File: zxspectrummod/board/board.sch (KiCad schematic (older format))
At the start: 7 parts, among them IC1 LVC245A, IC2 LVC245A

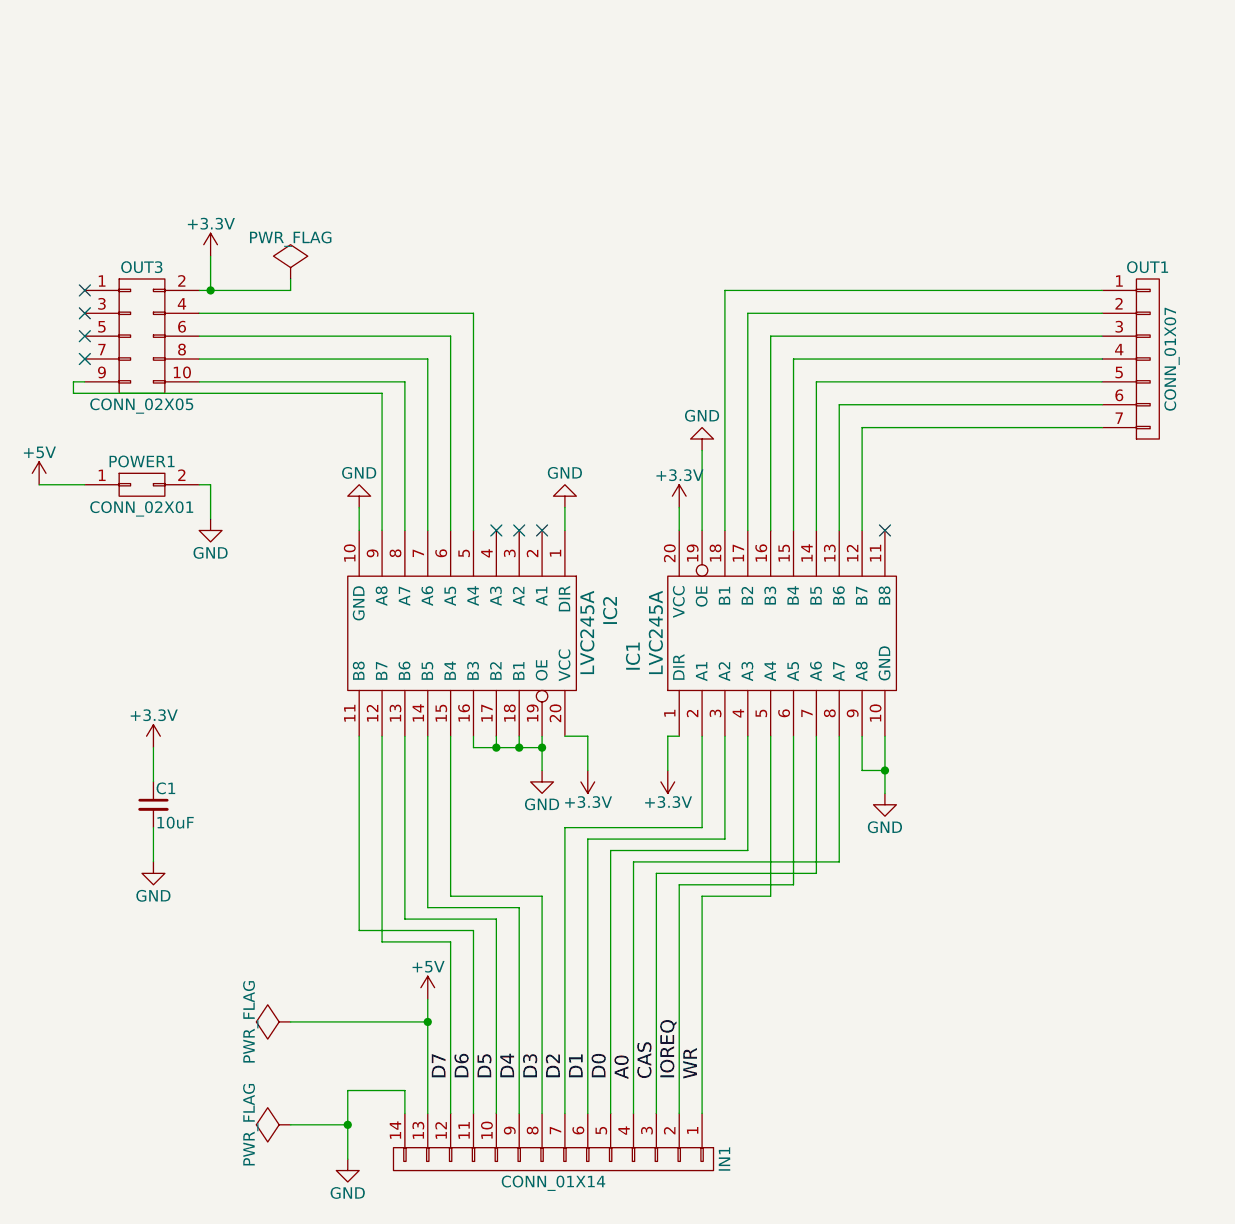
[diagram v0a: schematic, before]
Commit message: small additions for zx spectrum mod
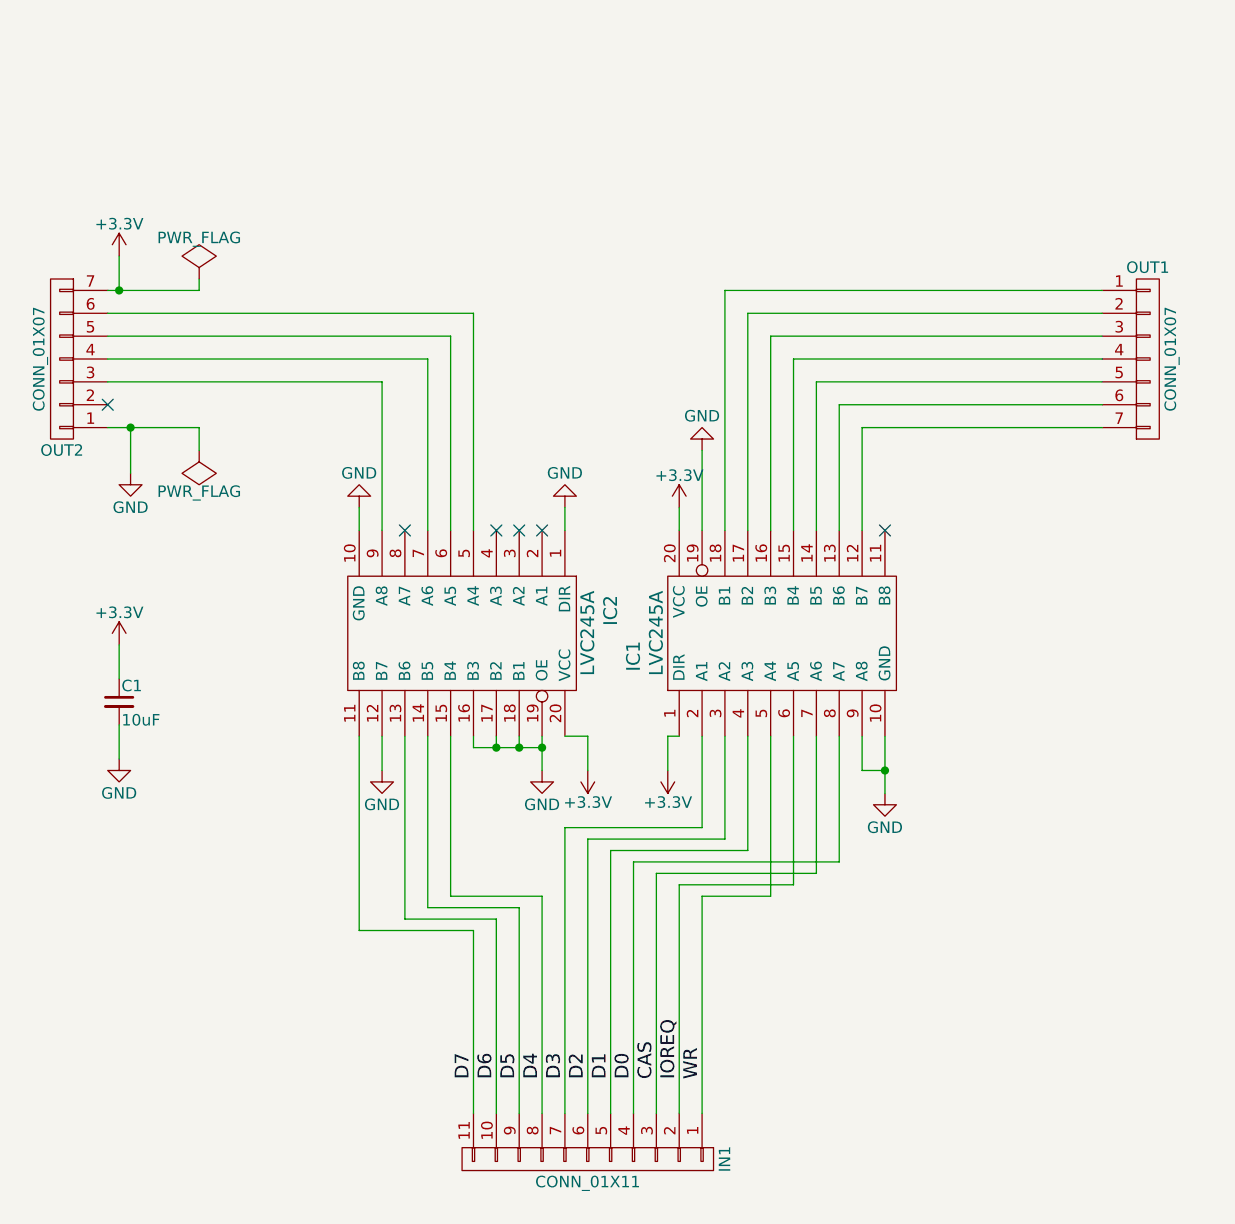
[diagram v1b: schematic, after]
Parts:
- removed IN1: CONN_01X14, Pin_Headers:Pin_Header_Straight_1x14_Pitch2.54mm, symbol CONN_01X14
- removed OUT3: CONN_02X05, Pin_Headers:Pin_Header_Straight_2x05_Pitch2.54mm, symbol CONN_02X05
- removed POWER1: CONN_02X01, Pin_Headers:Pin_Header_Straight_2x01_Pitch2.54mm, symbol CONN_02X01
- added IN1: CONN_01X11, Pin_Headers:Pin_Header_Straight_1x11_Pitch2.54mm, symbol CONN_01X11
- added OUT2: CONN_01X07, Pin_Headers:Pin_Header_Straight_1x07_Pitch2.54mm, symbol CONN_01X07
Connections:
- net A0 is gone; now on net D0: IC1.8 (A7)
- net +3V3: now also OUT2.7 (P7)
- net CAS: now also IN1.3 (P3)
- net D0: now also IN1.4 (P4); no longer IC1.4 (A3)
- net D1: now also IC1.4 (A3), IN1.5 (P5); no longer IC1.3 (A2)
- net D2: now also IC1.3 (A2), IN1.6 (P6); no longer IC1.2 (A1)
- net D3: now also IC1.2 (A1), IN1.7 (P7); no longer IC2.15 (B4)
- net D4: now also IC2.15 (B4), IN1.8 (P8); no longer IC2.14 (B5)
- net D5: now also IC2.14 (B5), IN1.9 (P9); no longer IC2.13 (B6)
- net D6: now also IC2.13 (B6), IN1.10 (P10); no longer IC2.11 (B8)
- net D7: now also IC2.11 (B8), IN1.11 (P11); no longer IC2.12 (B7)
- net GND: now also IC2.12 (B7), OUT2.1 (P1)
- net IOREQ: now also IN1.2 (P2)
- net WR: now also IN1.1 (P1)
- net at IC2.5 (A4): now also OUT2.6 (P6)
- net at IC2.6 (A5): now also OUT2.5 (P5)
- net at IC2.7 (A6): now also OUT2.4 (P4)
- net at IC2.9 (A8): now also OUT2.3 (P3)
- no-connect marks 8 -> 6
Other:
- moved on the sheet: C1

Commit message: Redesign ZX Spectrum Mod
To match the Rev.2 A-Video board
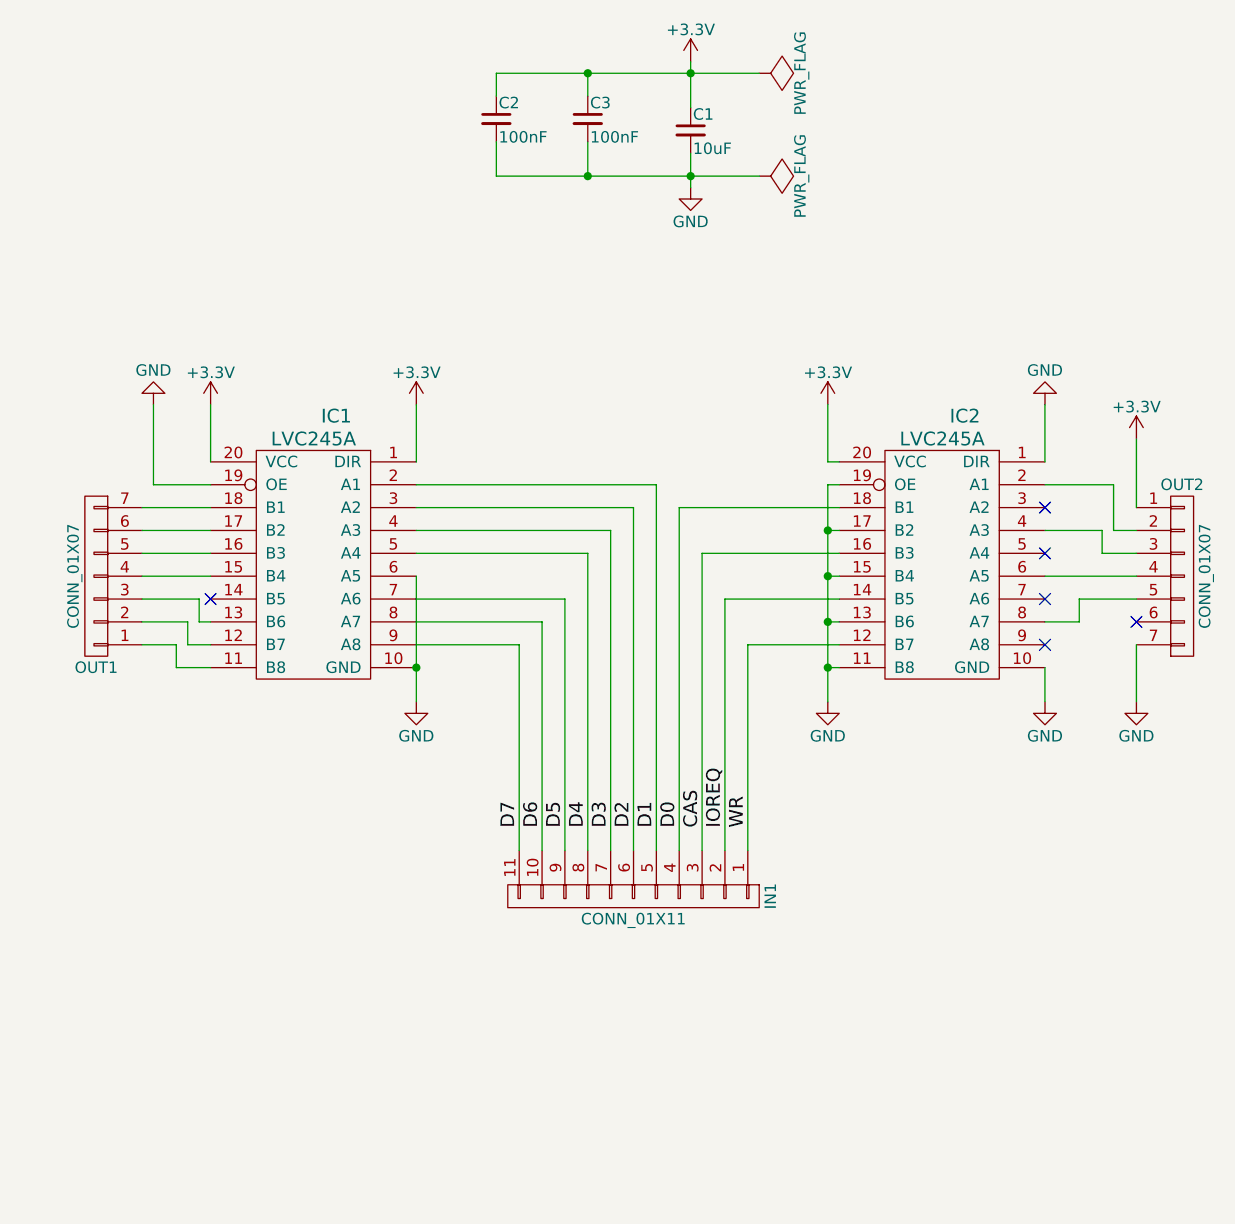
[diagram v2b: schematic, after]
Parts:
- added C2, C3: 100nF, Capacitors_SMD:C_0603_HandSoldering, symbol C_Small
- renumbered IC2 to IC1, IC1 to IC2
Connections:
- net +3V3: now also IC1.1 (DIR), OUT2.1 (P1), C2.1, C3.1; no longer IC2.1 (DIR), OUT2.7 (P7)
- net CAS: now also IC2.16 (B3); no longer IC2.7 (A6)
- net D0: now also IC2.18 (B1); no longer IC2.8 (A7)
- net D1: now also IC1.2 (A1); no longer IC2.4 (A3)
- net D2: now also IC1.3 (A2); no longer IC2.3 (A2)
- net D3: now also IC1.4 (A3); no longer IC2.2 (A1)
- net D4: now also IC1.5 (A4); no longer IC1.15 (B4)
- net D5: now also IC1.7 (A6); no longer IC1.14 (B5)
- net D6: now also IC1.8 (A7); no longer IC1.13 (B6)
- net D7: now also IC1.9 (A8); no longer IC1.11 (B8)
- net GND: now also IC1.6 (A5), IC2.1 (DIR), IC2.11 (B8), IC2.13 (B6), IC2.15 (B4), IC2.17 (B2), OUT2.7 (P7), C2.2, C3.2; no longer IC1.1 (DIR), IC1.12 (B7), IC1.16 (B3), IC1.17 (B2), IC1.18 (B1), IC2.9 (A8), OUT2.1 (P1)
- net IOREQ: now also IC2.14 (B5); no longer IC2.6 (A5)
- net WR: now also IC2.12 (B7); no longer IC2.5 (A4)
- net at OUT1.1 (P1): now also IC1.11 (B8); no longer IC2.18 (B1)
- net at OUT1.2 (P2): now also IC1.12 (B7); no longer IC2.17 (B2)
- net at OUT1.3 (P3): now also IC1.13 (B6); no longer IC2.16 (B3)
- net at OUT1.4 (P4): now also IC1.15 (B4); no longer IC2.15 (B4)
- net at OUT1.5 (P5): now also IC1.16 (B3); no longer IC2.14 (B5)
- net at OUT1.6 (P6): now also IC1.17 (B2); no longer IC2.13 (B6)
- net at OUT1.7 (P7): now also IC1.18 (B1); no longer IC2.12 (B7)
- net at OUT2.6 (P6): no longer IC1.5 (A4)
- net at OUT2.5 (P5): now also IC2.8 (A7); no longer IC1.6 (A5)
- net at OUT2.4 (P4): now also IC2.6 (A5); no longer IC1.7 (A6)
- net at OUT2.3 (P3): now also IC2.4 (A3); no longer IC1.9 (A8)
- net at OUT2.2 (P2): now also IC2.2 (A1)
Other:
- moved on the sheet: C1, IC1, IC2, IN1, OUT1, OUT2
